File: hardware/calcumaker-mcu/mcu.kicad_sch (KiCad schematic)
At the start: 14 parts, among them U1 STM32U575RGT6

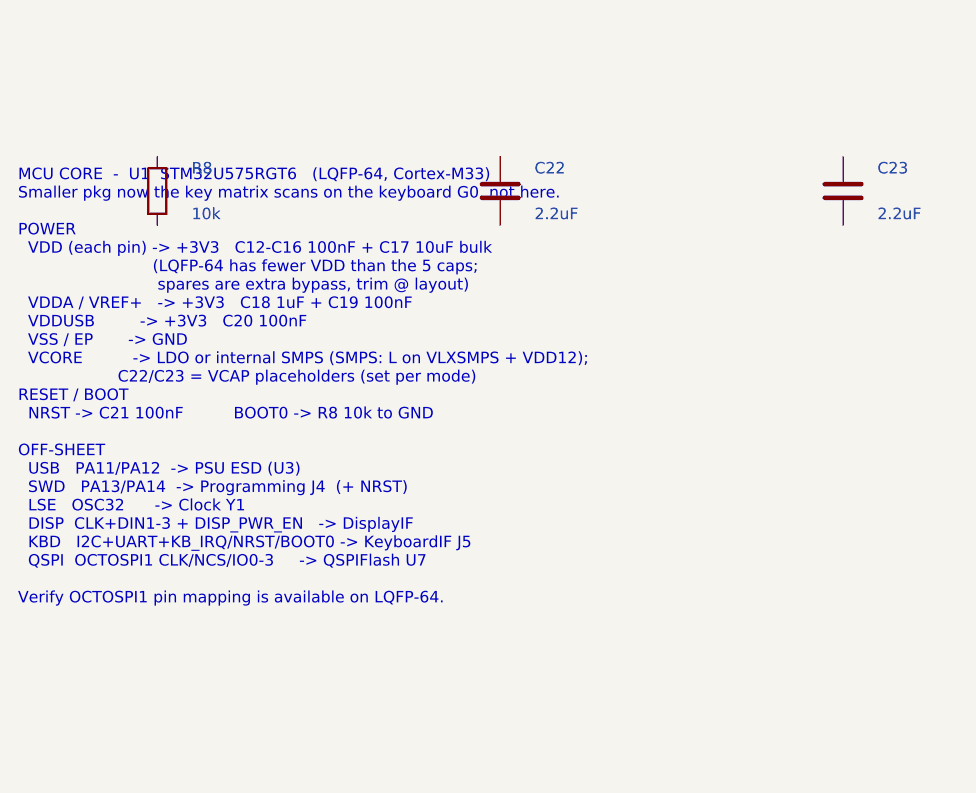
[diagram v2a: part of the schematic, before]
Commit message: hardware: per-key RGB hint lighting on the keyboard board (50x SK6805 on gated VSYS) (#4)
Add addressable RGB accent lighting that hints key positions / presses -- one
SK6805-EC15 (1.5x1.5mm, the smallest serial RGB with a KiCad footprint + real
LCSC stock, C2890035) beside each of the 50 keys, single-wire daisy chain off
one STM32G0 pin.

Power: the LEDs are ~5V parts and the keyboard rail is only 3.3V, so they run
off VSYS (the MCU board's load-shared battery/USB rail, ~3.7-4.7V) brought up a
WIDENED 12-pin mezzanine (10 -> 12: +VSYS +GND). A high-side P-FET load switch
(Q1 AO3401A + Q2 2N7002) gates the whole LED rail off in sleep (G0 LED_EN) to
protect battery life, and a 74LVC1G125 (powered from the gated rail) level-shifts
the 3.3V data up to the LED VIH.

- calcumaker-keyboard: new KeyLighting sheet (50x SK6805 D56-D105 + U2 shifter +
  Q1/Q2 load switch + R7-R10 / C6-C7); J1 mezzanine -> 12-pin DF40C-12DP
  (C6224952). 119 -> 178 components.
- calcumaker-mcu: J5 mezzanine -> 12-pin DF40B-12DS (C3641147); route VSYS.
- DF40 stack: the receptacle SUFFIX sets the mated height (none = 1.5mm,
  (2.0) = 2.0mm, H-series = 2.5-4.0mm), NOT the B/C letter; the DF40C plug is the
  common header -- so DF40C-12DP x DF40B-12DS is a valid 1.5mm stack, same as the
  original 10-pin (DF40C-12DS just isn't LCSC-stocked).
- DESIGN.md / PARTS.md / memory: RGB subsystem, 12-pin pinout, BOM rows, the
  sleep-gate + current-cap notes (firmware must cap total brightness; 50x
  full-white ~0.75A would exceed the DF40 / VSYS budget).

All three boards regenerate + pass the structure check (mcu 55 / keyboard 178 /
display 60, no duplicate refs).

Co-authored-by: Claude Opus 4.8 (1M context) <noreply@anthropic.com>
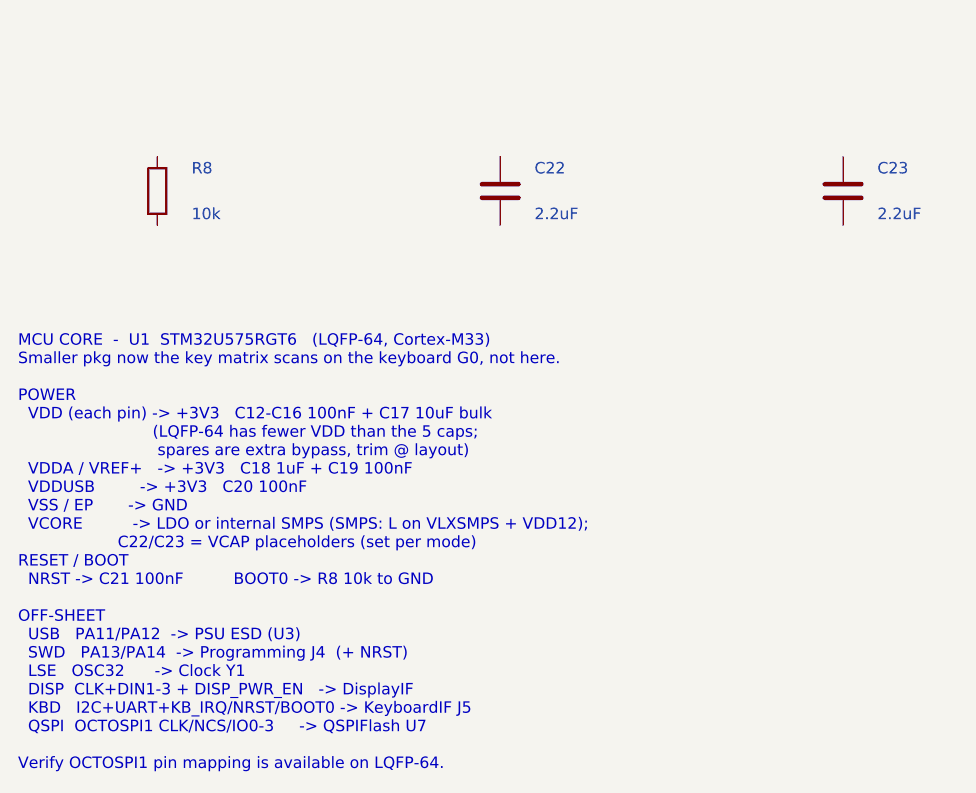
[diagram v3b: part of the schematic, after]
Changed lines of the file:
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@@
 	(text "MCU CORE  -  U1  STM32U575RGT6   (LQFP-64, Cortex-M33)\nSmaller pkg now the key matrix scans on the keyboard G0, not here.\n\nPOWER\n  VDD (each pin) -> +3V3   C12-C16 100nF + C17 10uF bulk\n                           (LQFP-64 has fewer VDD than the 5 caps;\n                            spares are extra bypass, trim @ layout)\n  VDDA / VREF+   -> +3V3   C18 1uF + C19 100nF\n  VDDUSB         -> +3V3   C20 100nF\n  VSS / EP       -> GND\n  VCORE          -> LDO or internal SMPS (SMPS: L on VLXSMPS + VDD12);\n                    C22/C23 = VCAP placeholders (set per mode)\nRESET / BOOT\n  NRST -> C21 100nF          BOOT0 -> R8 10k to GND\n\nOFF-SHEET\n  USB   PA11/PA12  -> PSU ESD (U3)\n  SWD   PA13/PA14  -> Programming J4  (+ NRST)\n  LSE   OSC32      -> Clock Y1\n  DISP  CLK+DIN1-3 + DISP_PWR_EN   -> DisplayIF\n  KBD   I2C+UART+KB_IRQ/NRST/BOOT0 -> KeyboardIF J5\n  QSPI  OCTOSPI1 CLK/NCS/IO0-3     -> QSPIFlash U7\n\nVerify OCTOSPI1 pin mapping is available on LQFP-64."
 		(exclude_from_sim no)
-		(at 15.00 150.00 0)
+		(at 15.00 168.40 0)
 		(effects (font (face "Courier New") (size 1.27 1.27)) (justify left top))
 	)

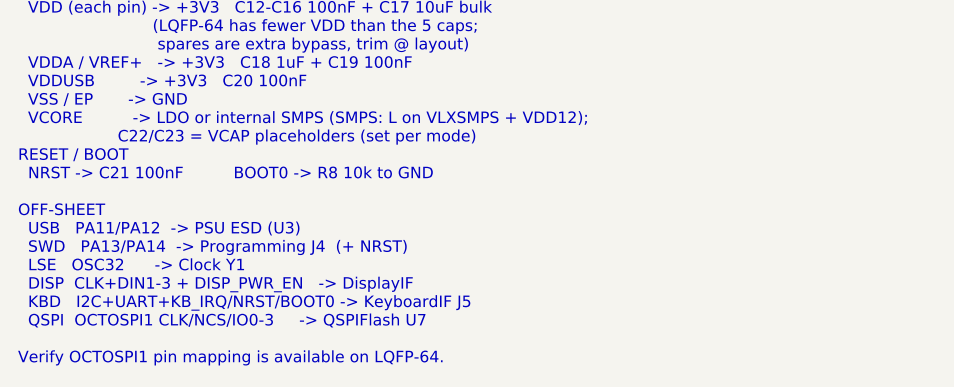
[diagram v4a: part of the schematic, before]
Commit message: hardware: unified SPI display-module interface + RGB dot-matrix board
Make the display a swappable module on ONE technology-agnostic connector
(mirrors the keyboard-G0 pattern): the MCU board speaks a single SPI
"display intent" bus and each display board carries its own MCU that
renders locally. Two interchangeable modules on the same 12-pin FFC.

- calcumaker-matrix (NEW): full-color RGB dot matrix, 96x24 = 2304x 1mm
  XL-1010RGBC-2812B-S (C51900942) driven by an RP2040 (PIO). Nested
  multi-channel: led_cluster (8x8) x12 -> led_row (768px chain) x3.
  Dedicated VSYS LED-power inlet keeps amps off the signal FFC. Authored
  the 1mm 1010 footprint; RP2040/flash/shifter symbols are stock.
- calcumaker-display (7-seg): retrofit to a smart module -- added an
  STM32G031 SPI slave, and moved the 5V boost (TPS61022) + 74HCT125
  shifter off the MCU board onto it. Interconnect reworked CLK/DIN -> SPI.
- calcumaker-mcu: DisplayIF simplified to the unified SPI connector +
  a 2-pin VSYS outlet for the matrix LED rail.

Unified pinout (mcu J3 / display J1 / matrix J1): VSYS,VSYS,GND,GND,+3V3,
SPI_SCLK,SPI_MOSI,SPI_CS,DISP_IRQ,DISP_NRST,DISP_BOOT,GND.

All boards generate + check clean (mcu 46 / keyboard 179 / display 77 /
matrix 2339, no dup refs). Docs (PARTS.md, DESIGN.md, Makefile) updated.
Firmware is deferred; the SPI contract is documented so it is unblocked.

Co-Authored-By: Claude Opus 4.8 (1M context) <noreply@anthropic.com>
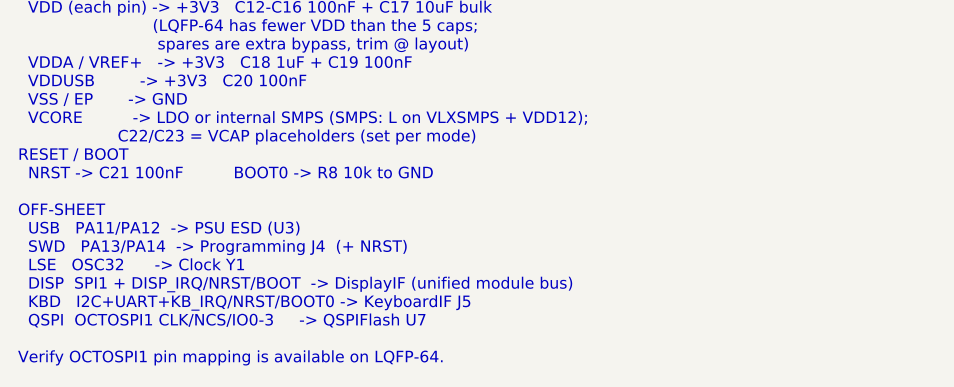
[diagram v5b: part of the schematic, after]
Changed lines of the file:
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@@
 		)
 	)
-	(text "MCU CORE  -  U1  STM32U575RGT6   (LQFP-64, Cortex-M33)\nSmaller pkg now the key matrix scans on the keyboard G0, not here.\n\nPOWER\n  VDD (each pin) -> +3V3   C12-C16 100nF + C17 10uF bulk\n                           (LQFP-64 has fewer VDD than the 5 caps;\n                            spares are extra bypass, trim @ layout)\n  VDDA / VREF+   -> +3V3   C18 1uF + C19 100nF\n  VDDUSB         -> +3V3   C20 100nF\n  VSS / EP       -> GND\n  VCORE          -> LDO or internal SMPS (SMPS: L on VLXSMPS + VDD12);\n                    C22/C23 = VCAP placeholders (set per mode)\nRESET / BOOT\n  NRST -> C21 100nF          BOOT0 -> R8 10k to GND\n\nOFF-SHEET\n  USB   PA11/PA12  -> PSU ESD (U3)\n  SWD   PA13/PA14  -> Programming J4  (+ NRST)\n  LSE   OSC32      -> Clock Y1\n  DISP  CLK+DIN1-3 + DISP_PWR_EN   -> DisplayIF\n  KBD   I2C+UART+KB_IRQ/NRST/BOOT0 -> KeyboardIF J5\n  QSPI  OCTOSPI1 CLK/NCS/IO0-3     -> QSPIFlash U7\n\nVerify OCTOSPI1 pin mapping is available on LQFP-64."
+	(text "MCU CORE  -  U1  STM32U575RGT6   (LQFP-64, Cortex-M33)\nSmaller pkg now the key matrix scans on the keyboard G0, not here.\n\nPOWER\n  VDD (each pin) -> +3V3   C12-C16 100nF + C17 10uF bulk\n                           (LQFP-64 has fewer VDD than the 5 caps;\n                            spares are extra bypass, trim @ layout)\n  VDDA / VREF+   -> +3V3   C18 1uF + C19 100nF\n  VDDUSB         -> +3V3   C20 100nF\n  VSS / EP       -> GND\n  VCORE          -> LDO or internal SMPS (SMPS: L on VLXSMPS + VDD12);\n                    C22/C23 = VCAP placeholders (set per mode)\nRESET / BOOT\n  NRST -> C21 100nF          BOOT0 -> R8 10k to GND\n\nOFF-SHEET\n  USB   PA11/PA12  -> PSU ESD (U3)\n  SWD   PA13/PA14  -> Programming J4  (+ NRST)\n  LSE   OSC32      -> Clock Y1\n  DISP  SPI1 + DISP_IRQ/NRST/BOOT  -> DisplayIF (unified module bus)\n  KBD   I2C+UART+KB_IRQ/NRST/BOOT0 -> KeyboardIF J5\n  QSPI  OCTOSPI1 CLK/NCS/IO0-3     -> QSPIFlash U7\n\nVerify OCTOSPI1 pin mapping is available on LQFP-64."
 		(exclude_from_sim no)
 		(at 15.00 168.40 0)

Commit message: hw: assign the OCTOSPI1 pinout and fold Clock/Prog/DisplayIF into MCU
The MCU sheet carried a "verify OCTOSPI1 pin mapping is available on
LQFP-64" TODO and the flash sheet said to assign it "to the PB/PC bank".
Both are now settled, and the PB/PC hint was wrong.

On the U5 the OCTOSPI GPIOs belong to the OCTOSPI I/O manager, so the AF
signals are OCTOSPIM_P1_*/P2_*. LQFP-64 bonds out no Port-2 bus at all
(ports E/F/G absent; only P2_NCS is present), so Port 1 is mandatory —
and on Port 1 IO0..IO3 each have exactly one candidate pin. Only CLK
(PA3|PB10) and NCS (PA2|PA4|PC11) were a real choice:

  CLK PB10 AF10 p29   IO0 PB1 AF10 p27   IO2 PA7 AF10 p23
  NCS PA4  AF3  p20   IO1 PB0 AF10 p26   IO3 PA6 AF10 p22

PB10+PA4 keep the whole bus in a contiguous pin 20-29 cluster (short and
length-matchable for >=50 MHz quad) and leave PA2/PA3 whole as the USART2
TX/RX pair for the keyboard link. It costs SPI1_NSS and WKUP2, both of
which have alternates. Every pin is verified against ST's package-filtered
CubeMX pin database for STM32U575RGTx / LQFP-64.

Taking PA6/PA7 for the flash consumes SPI1_MISO/MOSI, so the display
module bus moves to SCK=PA5, MOSI=PB5, CS=PA15. No MISO is needed — the
12-pin FFC doesn't carry one.

Sheet surgery: Clock (Y1 + C24/C25), Programming (J4) and DisplayIF
(J3 + J7) were already merged into the MCU sheet, leaving three files
unreferenced from the root. Delete them. The notes were edited in place
rather than regenerated, so the manual eeschema wiring survives; the
structure check reports the same 46 components and the same ERC tally as
before the change.

Also fix two things DESIGN.md got wrong on the way past:
  - The Power Tree still showed a 5V boost gated by DISP_PWR_EN and a
    74HCT125 on the MCU board. Those parts live on the display module now
    (DESIGN.md says so elsewhere) and exist on no sheet here; the PSU has
    only the TPS63900. VSYS passes through raw to J3/J7.
  - The board is 46 components, not 55.

Still open: KB_IRQ 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
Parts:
- added C24, C25: 12pF, Capacitor_SMD:C_0402_1005Metric, symbol Device:C
- added J3: TO DISPLAY (unified SPI FFC), Connector_FFC-FPC:Hirose_FH12-12S-0.5SH_1x12-1MP_P0.50mm_Horizontal, symbol Connector_Generic:Conn_01x12
- added J4: SWD TC2030-NL, Connector:Tag-Connect_TC2030-IDC-NL_2x03_P1.27mm_Vertical, symbol Connector:Conn_ARM_SWD_TagConnect_TC2030-NL
- added J7: VSYS -> matrix LED pwr, Connector_JST:JST_PH_S2B-PH-K_1x02_P2.00mm_Horizontal, symbol Connector_Generic:Conn_01x02
- added Y1: 32.768kHz, Crystal:Crystal_SMD_3215-2Pin_3.2x1.5mm, symbol Device:Crystal
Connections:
- net VDDUSB: now reaches C20.1
- net VDDUSB: now also U1.48 (VDDUSB)
- net GND: now reaches C20.2
- net GND: now also U1.12 (VSSA), U1.18 (VSS), U1.31 (VSS), U1.47 (VSS), U1.63 (VSS)
- net VDD: now reaches U1.13 (VDDA)
- net VDD: now also U1.19 (VDD), U1.32 (VDD), U1.64 (VDD)
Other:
- note added: "CLOCK - LSE 32.768 kHz (Y1 Q13FC13500004, LCSC C32346) Y1.1 -> OSC32_IN (PC14) Y1.2 -> OSC32_OUT (PC15) C24 / C25 -> LSE load caps to GND (12pF shown) Load caps: CL match = 2*(CL - Cstray); trim with the RTC SMOOTHCALIB. Drives the RTC for sleep timing."
- note added: "SWD PROGRAMMING - J4 Tag-Connect TC2030-NL (no-legs pogo pad) Bare land, no part mounted. PIN SIGNAL 1 +3V3 (VTref) 2 SWDIO (PA13) 3 NRST 4 SWCLK (PA14) 5 GND 6 SWO (PB3, opt)"
- note added: "UNIFIED DISPLAY-MODULE INTERFACE J3 = 0.5mm 12-pos FFC to the display module (AFC01-S12FCA-00, C262661). SAME pinout on BOTH display boards (7-seg + RGB matrix) -> interchangeable. Technology-agnostic: power + SPI 'display intent' + reset/boot. The module MCU (STM32G031 on 7-seg / RP2040 on the matrix) is the SPI slave + renders locally; 5V + any level-shifting are generated ON the module now. PI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"
- moved on the sheet: C20, U1
